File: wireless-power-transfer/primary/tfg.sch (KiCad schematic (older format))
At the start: 35 parts, among them J1 CONN_01X06, J2 Screw_Terminal_1x02, J3 BARREL_JACK, Q1 IRLB8721PBF, Q2 IRLB8721PBF, Q3 IRLB8721PBF, Q4 IRLB8721PBF, U1 PIC18F45K20-I/PT, U2 IR2110, U3 IR2110, U4 R-78E15, U5 R-78E3.3, U6 XBEE_Wi-Fi

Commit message: Added pdf sheets and modified layout according with the school standard for TFGs.
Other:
- note added: "1/3"
- moved on the sheet: 47uH1, C1, C2, C5, C6, C7, Cboot1, Cboot2, Cf1, Cf2, Cr1, Cr2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

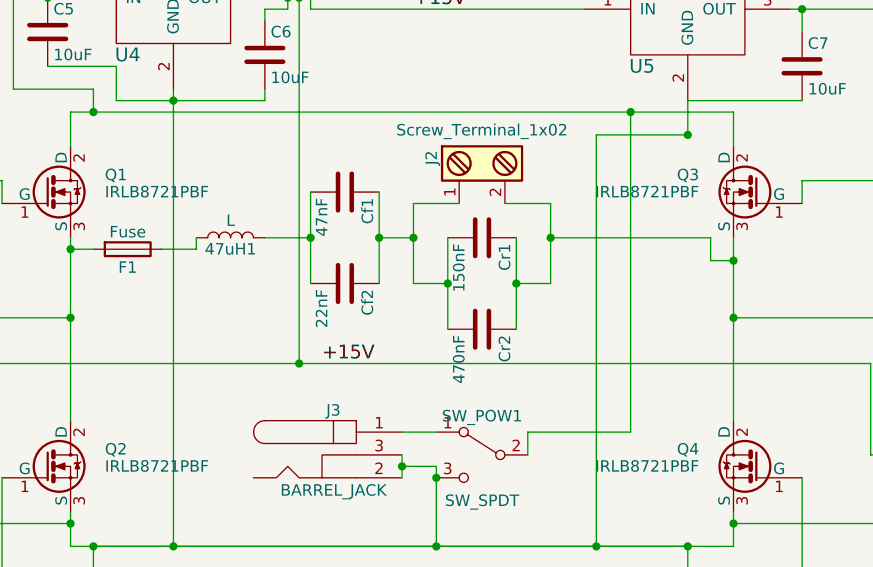
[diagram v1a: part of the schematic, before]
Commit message: PCB modified extracting the filter and the tank to another PCB.
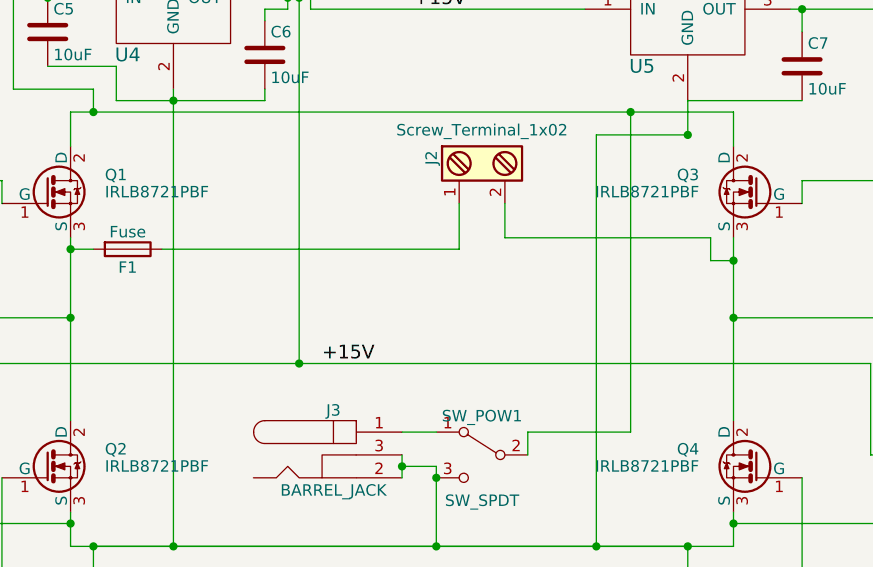
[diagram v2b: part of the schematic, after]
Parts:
- removed 47uH1: L, Choke_SMD:Choke_SMD_12x12mm_h6mm, symbol L
- removed Cf1: 47nF, Capacitors_THT:C_Rect_L18.0mm_W5.0mm_P15.00mm_FKS3_FKP3, symbol C
- removed Cf2: 22nF, Capacitors_THT:C_Rect_L13.0mm_W5.0mm_P10.00mm_FKS3_FKP3_MKS4, symbol C
- removed Cr1: 150nF, Capacitors_THT:C_Rect_L7.2mm_W2.5mm_P5.00mm_FKS2_FKP2_MKS2_MKP2, symbol C
- removed Cr2: 470nF, Capacitors_THT:C_Rect_L18.0mm_W11.0mm_P15.00mm_FKS3_FKP3, symbol C
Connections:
- net at J2.1: now also F1.1
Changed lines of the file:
@@
 Wire Wire Line
 	6750 3050 10900 3050
-Wire Wire Line
-	8400 3050 8400 1450
 Connection ~ 8400 1450
 Wire Wire Line
@@
 Wire Wire Line
 	8450 1500 8450 1450
-$Comp
-L C Cr1
-U 1 1 59DF6A05
-P 9200 2500
-F 0 "Cr1" H 9225 2600 50  0000 L CNN
-F 1 "150nF" H 9225 2400 50  0000 L CNN
-F 2 "Capacitors_THT:C_Rect_L7.2mm_W2.5mm_P5.00mm_FKS2_FKP2_MKS2_MKP2" H 9238 2350 50  0001 C CNN
-F 3 "" H 9200 2500 50  0001 C CNN
-	1    9200 2500
-	0    1    1    0
-$EndComp
 $Comp
 L Screw_Terminal_1x02 J2
@@
 $EndComp
 Wire Wire Line
-	9100 2350 8900 2350
-Wire Wire Line
-	8900 2350 8900 2700
-Wire Wire Line
-	8900 2700 9050 2700
-Wire Wire Line
-	9350 2700 9500 2700
-Wire Wire Line
-	9500 2700 9500 2350
-Wire Wire Line
-	9500 2350 9300 2350
-$Comp
-L C Cf1
-U 1 1 59DF6CD9
-P 8600 2300
-F 0 "Cf1" H 8625 2400 50  0000 L CNN
-F 1 "47nF" H 8625 2200 50  0000 L CNN
-F 2 "Capacitors_THT:C_Rect_L18.0mm_W5.0mm_P15.00mm_FKS3_FKP3" H 8638 2150 50  0001 C CNN
-F 3 "" H 8600 2300 50  0001 C CNN
-	1    8600 2300
-	0    1    1    0
-$EndComp
-$Comp
-L L 47uH1
-U 1 1 59DF6D3C
-P 8100 2500
-F 0 "47uH1" V 8050 2500 50  0000 C CNN
-F 1 "L" V 8175 2500 50  0000 C CNN
-F 2 "Choke_SMD:Choke_SMD_12x12mm_h6mm" H 8100 2500 50  0001 C CNN
-F 3 "" H 8100 2500 50  0001 C CNN
-	1    8100 2500
-	0    -1   -1   0
-$EndComp
-Wire Wire Line
-	8250 2500 8450 2500
-Wire Wire Line
-	8750 2500 8900 2500
-Connection ~ 8900 2500
-Wire Wire Line
-	9500 2500 10200 2500
-Wire Wire Line
 	10200 2500 10200 2600
 Wire Wire Line
 	10200 2600 10300 2600
 Connection ~ 10300 2600
-Connection ~ 9500 2500
 Connection ~ 7400 2550
 $Comp
@@
 	10600 1900 10100 1900
 $Comp
-L C Cf2
-U 1 1 59E09138
-P 8600 2700
-F 0 "Cf2" H 8625 2800 50  0000 L CNN
-F 1 "22nF" H 8625 2600 50  0000 L CNN
-F 2 "Capacitors_THT:C_Rect_L13.0mm_W5.0mm_P10.00mm_FKS3_FKP3_MKS4" H 8638 2550 50  0001 C CNN
-F 3 "" H 8600 2700 50  0001 C CNN
-	1    8600 2700
-	0    1    1    0
-$EndComp
-Wire Wire Line
-	8450 2300 8450 2700
-Connection ~ 8450 2500
-Wire Wire Line
-	8750 2300 8750 2700
-Connection ~ 8750 2500
-$Comp
-L C Cr2
-U 1 1 59E0962F
-P 9200 2900
-F 0 "Cr2" H 9225 3000 50  0000 L CNN
-F 1 "470nF" H 9225 2800 50  0000 L CNN
-F 2 "Capacitors_THT:C_Rect_L18.0mm_W11.0mm_P15.00mm_FKS3_FKP3" H 9238 2750 50  0001 C CNN
-F 3 "" H 9200 2900 50  0001 C CNN
-	1    9200 2900
-	0    1    1    0
-$EndComp
-Wire Wire Line
-	9050 2500 9050 2900
-Connection ~ 9050 2700
-Wire Wire Line
-	9350 2500 9350 2900
-Connection ~ 9350 2700
-$Comp
 L SW_SPDT SW_POW1
 U 1 1 59E0D445
@@
 Wire Wire Line
 	7400 2550 7500 2550
-Wire Wire Line
-	7800 2550 7950 2550
-Wire Wire Line
-	7950 2550 7950 2500
 Wire Wire Line
 	11350 1400 13700 1400
@@
 Text Notes 14950 11050 0    197  ~ 0
 1/3
+Wire Wire Line
+	8400 3050 8400 1450
+Wire Wire Line
+	7800 2550 9100 2550
+Wire Wire Line
+	9100 2550 9100 2350
+Wire Wire Line
+	9300 2350 9300 2500
+Wire Wire Line
+	9300 2500 10200 2500
 $EndSCHEMATC

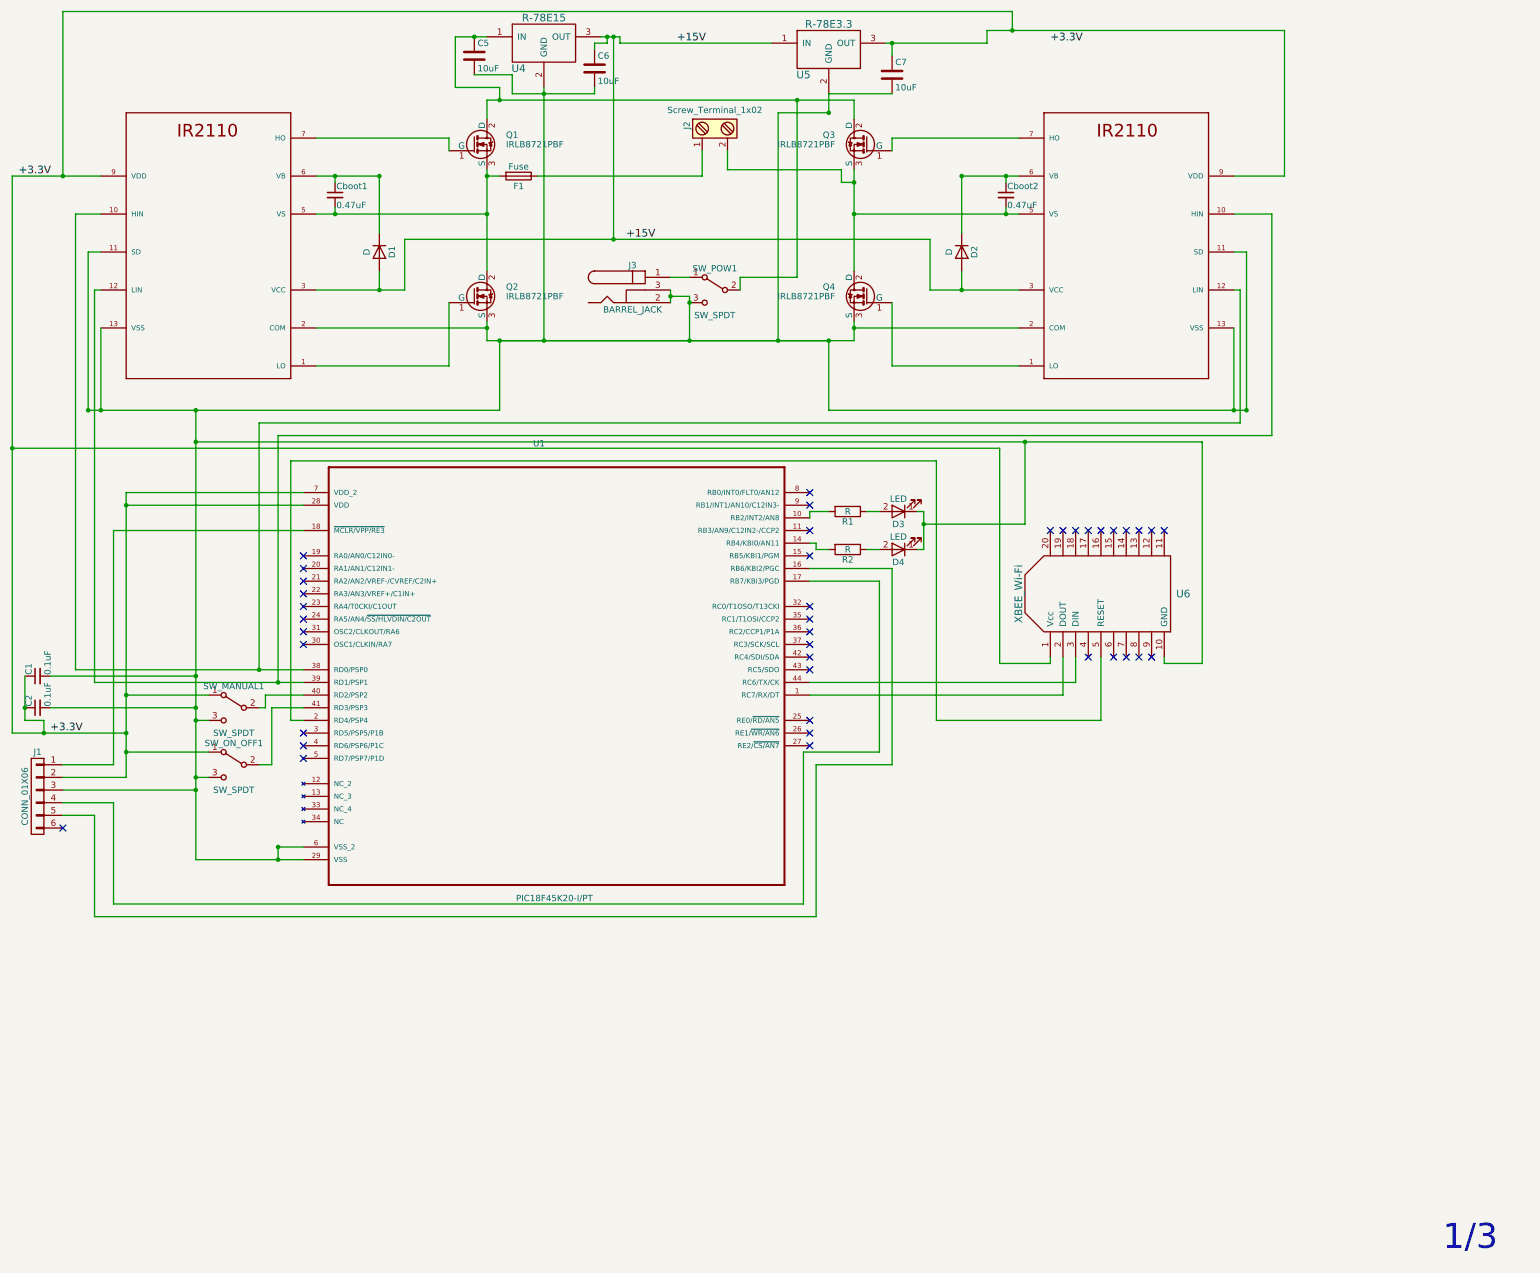
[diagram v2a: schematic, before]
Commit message: Added switch labels.
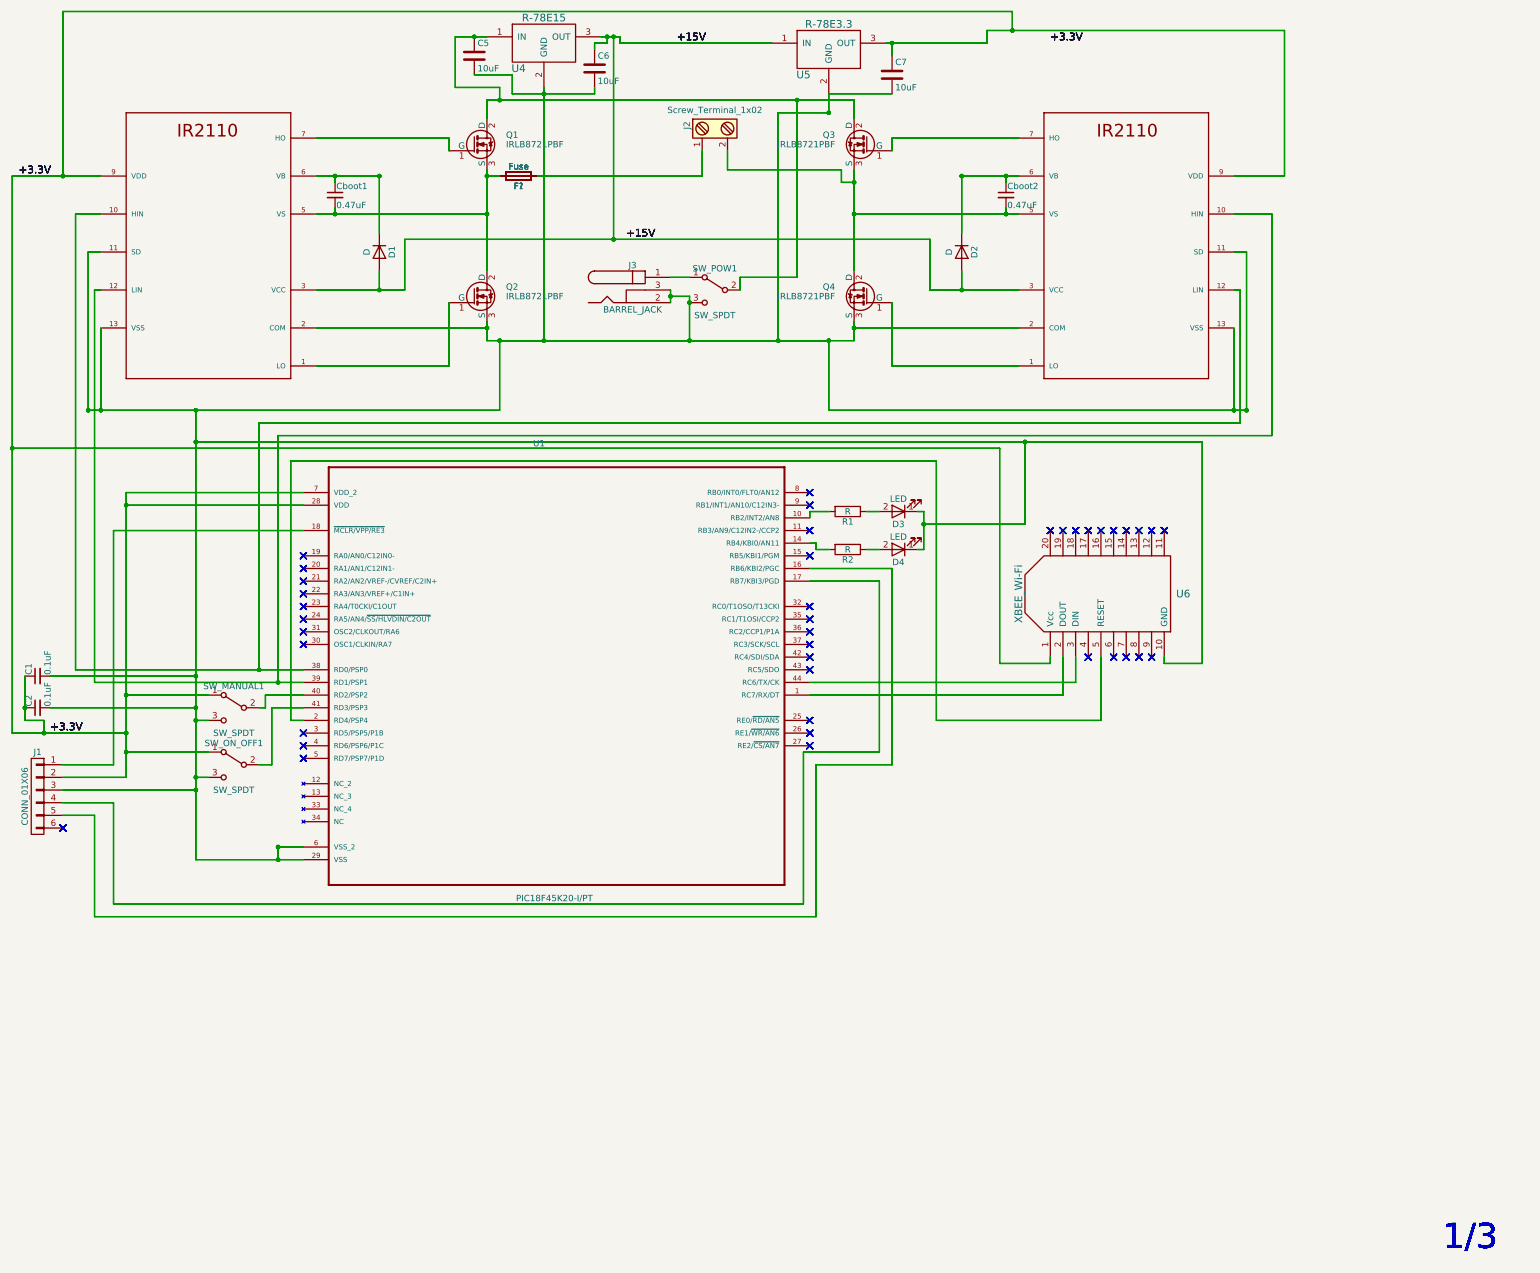
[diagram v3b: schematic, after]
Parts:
- added F? (x3): Fuse, Fuse_Holders_and_Fuses:Fuseholder5x20_horiz_SemiClosed_Casing10x25mm, symbol Fuse
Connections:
- net at Cboot1.2, F1.2, Q1.3 (S)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: now also F?.2, F?.2, F?.2
- net at F1.1, J2.1: now also F?.1, F?.1, F?.1
- no-connect marks 40 -> 160

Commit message: Added pcb with tank and filter of the primary, some logos and other minor changes.
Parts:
- removed F? (x3): Fuse, Fuse_Holders_and_Fuses:Fuseholder5x20_horiz_SemiClosed_Casing10x25mm, symbol Fuse
